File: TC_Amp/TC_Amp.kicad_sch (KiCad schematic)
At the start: 58 parts, among them J1 Screw_Terminal_01x02, J2 Screw_Terminal_01x02, J3 Conn_01x04_Pin, J4 Screw_Terminal_01x02, J5 Screw_Terminal_01x02, Q1 PMOS, U11 LM741, U12 LTC1049CN8_PBF, U13 LTC1049CN8_PBF, U14 LM317T, U15 LT1025CN8-PBF, U2 LTC1049CN8_PBF, U3 LT1054, U4 LM741, U5 LTC1049CN8_PBF, U7 LM741, U8 LTC1049CN8_PBF, U9 LTC1049CN8_PBF

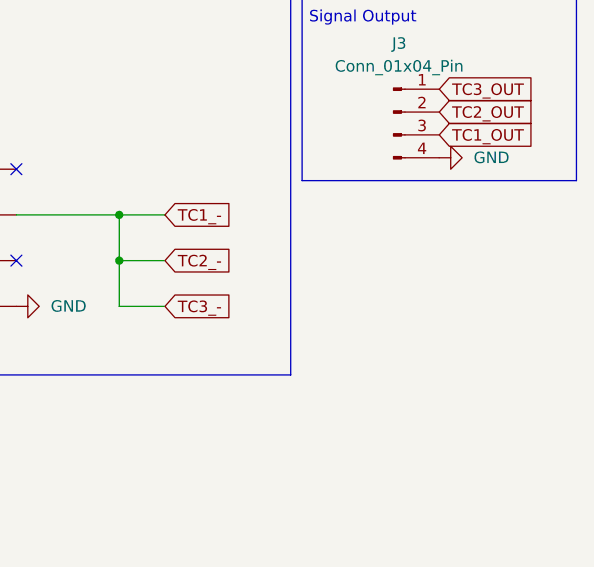
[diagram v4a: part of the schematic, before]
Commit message: rounded etch corners and added m3 holes
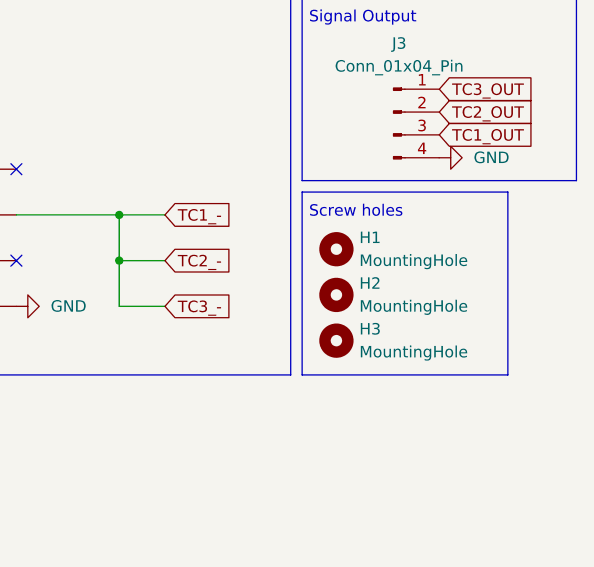
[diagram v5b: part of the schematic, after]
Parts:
- added H1, H2, H3: MountingHole, MountingHole:MountingHole_3.2mm_M3_DIN965, symbol Mechanical:MountingHole
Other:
- note added: "Screw holes"
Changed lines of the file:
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@@
 	)
 	(rectangle
+		(start 294.64 34.29)
+		(end 317.5 54.61)
+		(stroke
+			(width 0)
+			(type default)
+			(color 0 0 255 1)
+		)
+		(fill
+			(type none)
+		)
+	)
+	(rectangle
 		(start 59.69 12.7)
 		(end 135.89 60.96)
@@
 		)
 	)
+	(text "Screw holes"
+		(exclude_from_sim no)
+		(at 295.402 36.576 0)
+		(effects
+			(font
+				(size 1.27 1.27)
+				(color 0 0 255 1)
+			)
+			(justify left)
+		)
+	)
 	(text "As long as each pair of resistors are equal there is no gain \nand the output is the sum of the voltage inputs\nChose 10k for balance of power loss and signal integrity"
 		(exclude_from_sim no)
@@
 	)
 	(symbol
+		(lib_id "Mechanical:MountingHole")
+		(at 298.45 45.72 0)
+		(unit 1)
+		(exclude_from_sim yes)
+		(in_bom no)
+		(on_board yes)
+		(dnp no)
+		(fields_autoplaced yes)
+		(property "Reference" "H2"
+			(at 300.99 44.4499 0)
+			(effects
+				(font
+					(size 1.27 1.27)
+				)
+				(justify left)
+			)
+		)
+		(property "Value" "MountingHole"
+			(at 300.99 46.9899 0)
+			(effects
+				(font
+					(size 1.27 1.27)
+				)
+				(justify left)
+			)
+		)
+		(property "Footprint" "MountingHole:MountingHole_3.2mm_M3_DIN965"
+			(at 298.45 45.72 0)
+			(effects
+				(font
+					(size 1.27 1.27)
+				)
+				(hide yes)
+			)
+		)
+		(property "Datasheet" "~"
+			(at 298.45 45.72 0)
+			(effects
+				(font
+					(size 1.27 1.27)
+				)
+				(hide yes)
+			)
+		)
+		(property "Description" "Mounting Hole without connection"
+			(at 298.45 45.72 0)
+			(effects
+				(font
+					(size 1.27 1.27)
+				)
+				(hide yes)
+			)
+		)
+		(instances
+			(project "TC_Amp"
+				(path "/4930a40b-d9a2-42ec-982c-b1e056cf9c0f"
+					(reference "H2")
+					(unit 1)
+				)
+			)
+		)
+	)
+	(symbol
 		(lib_id "Device:C")
 		(at 123.19 44.45 0)
@@
 	)
 	(symbol
+		(lib_id "Mechanical:MountingHole")
+		(at 298.45 40.64 0)
+		(unit 1)
+		(exclude_from_sim yes)
+		(in_bom no)
+		(on_board yes)
+		(dnp no)
+		(fields_autoplaced yes)
+		(property "Reference" "H1"
+			(at 300.99 39.3699 0)
+			(effects
+				(font
+					(size 1.27 1.27)
+				)
+				(justify left)
+			)
+		)
+		(property "Value" "MountingHole"
+			(at 300.99 41.9099 0)
+			(effects
+				(font
+					(size 1.27 1.27)
+				)
+				(justify left)
+			)
+		)
+		(property "Footprint" "MountingHole:MountingHole_3.2mm_M3_DIN965"
+			(at 298.45 40.64 0)
+			(effects
+				(font
+					(size 1.27 1.27)
+				)
+				(hide yes)
+			)
+		)
+		(property "Datasheet" "~"
+			(at 298.45 40.64 0)
+			(effects
+				(font
+					(size 1.27 1.27)
+				)
+				(hide yes)
+			)
+		)
+		(property "Description" "Mounting Hole without connection"
+			(at 298.45 40.64 0)
+			(effects
+				(font
+					(size 1.27 1.27)
+				)
+				(hide yes)
+			)
+		)
+		(instances
+			(project ""
+				(path "/4930a40b-d9a2-42ec-982c-b1e056cf9c0f"
+					(reference "H1")
+					(unit 1)
+				)
+			)
+		)
+	)
+	(symbol
 		(lib_id "Device:R_Potentiometer_US")
 		(at 26.67 222.25 270)
@@
 					(unit 1)
 				)
+			)
+		)
+	)
+	(symbol
+		(lib_id "Mechanical:MountingHole")
+		(at 298.45 50.8 0)
+		(unit 1)
+		(exclude_from_sim yes)
+		(in_bom no)
+		(on_board yes)
+		(dnp no)
+		(fields_autoplaced yes)
+		(property "Reference" "H3"
+			(at 300.99 49.5299 0)
+			(effects
+				(font
+					(size 1.27 1.27)
+				)
+				(justify left)
+			)
+		)
+		(property "Value" "MountingHole"
+			(at 300.99 52.0699 0)
+			(effects
+				(font
+					(size 1.27 1.27)
+				)
+				(justify left)
+			)
+		)
+		(property "Footprint" "MountingHole:MountingHole_3.2mm_M3_DIN965"
+			(at 298.45 50.8 0)
+			(effects
+				(font
+					(size 1.27 1.27)
+				)
+				(hide yes)
+			)
+		)
+		(property "Datasheet" "~"
+			(at 298.45 50.8 0)
+			(effects
+				(font
+					(size 1.27 1.27)
+				)
+				(hide yes)
+			)
+		)
+		(property "Description" "Mounting Hole without connection"
+			(at 298.45 50.8 0)
+			(effects
+				(font
+					(size 1.27 1.27)
+				)
+				(hide yes)
+			)
+		)
+		(instances
+			(project "TC_Amp"
+				(path "/4930a40b-d9a2-42ec-982c-b1e056cf9c0f"
+					(reference "H3")
+					(unit 1)
+				)

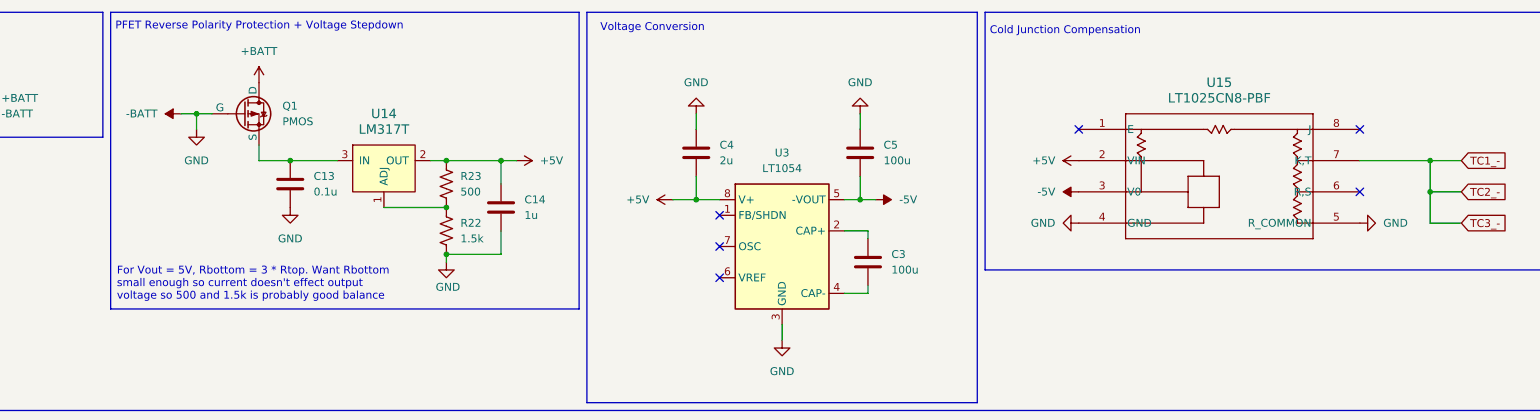
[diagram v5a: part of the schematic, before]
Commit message: updated schematic with physical changes
removed linear regulator to mandate 5v input, added 10k resistor to R- of CJC
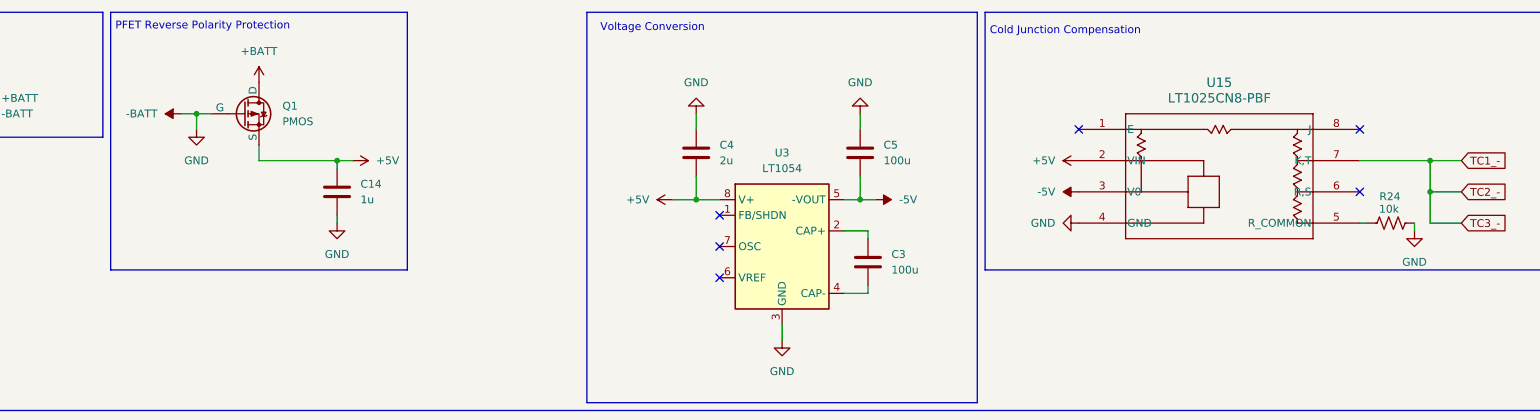
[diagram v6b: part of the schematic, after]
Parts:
- removed C13: 0.1u, Capacitor_THT:C_Radial_D5.0mm_H5.0mm_P2.00mm, symbol Device:C
- removed R22: 1.5k, Resistor_THT:R_Axial_DIN0207_L6.3mm_D2.5mm_P10.16mm_Horizontal, symbol Device:R_US
- removed R23: 500, Resistor_THT:R_Axial_DIN0207_L6.3mm_D2.5mm_P10.16mm_Horizontal, symbol Device:R_US
- removed U14: LM317T, digikey-footprints:TO-220-3, symbol dk_PMIC-Voltage-Regulators-Linear:LM317T
- added R24: 10k, Resistor_THT:R_Axial_DIN0207_L6.3mm_D2.5mm_P10.16mm_Horizontal, symbol Device:R_US
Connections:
- net +5V: now also Q1.3 (S)
- net -BATT: now also R24.2; no longer U15.5 (R_COMMON)
- new net: R24.1, U15.5 (R_COMMON)
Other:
- note added: "PFET Reverse Polarity Protection"
- note removed: "For Vout = 5V, Rbottom = 3 * Rtop. Want Rbottom small enough so current doesn't effect output voltage so 500 and 1.5k is probably good balance"
- note removed: "PFET Reverse Polarity Protection + Voltage Stepdown"
- moved on the sheet: C14
